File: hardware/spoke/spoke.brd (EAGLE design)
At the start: 45.7 x 44.1 mm, 23 parts, among them IC1 7805TV, IC2 LM3490, J1 AVR_SPI_PRG_6PTH, J2 POWER_JACKPTH, U1 ATMEGA328P_PDIP, U3 NRF24L01+

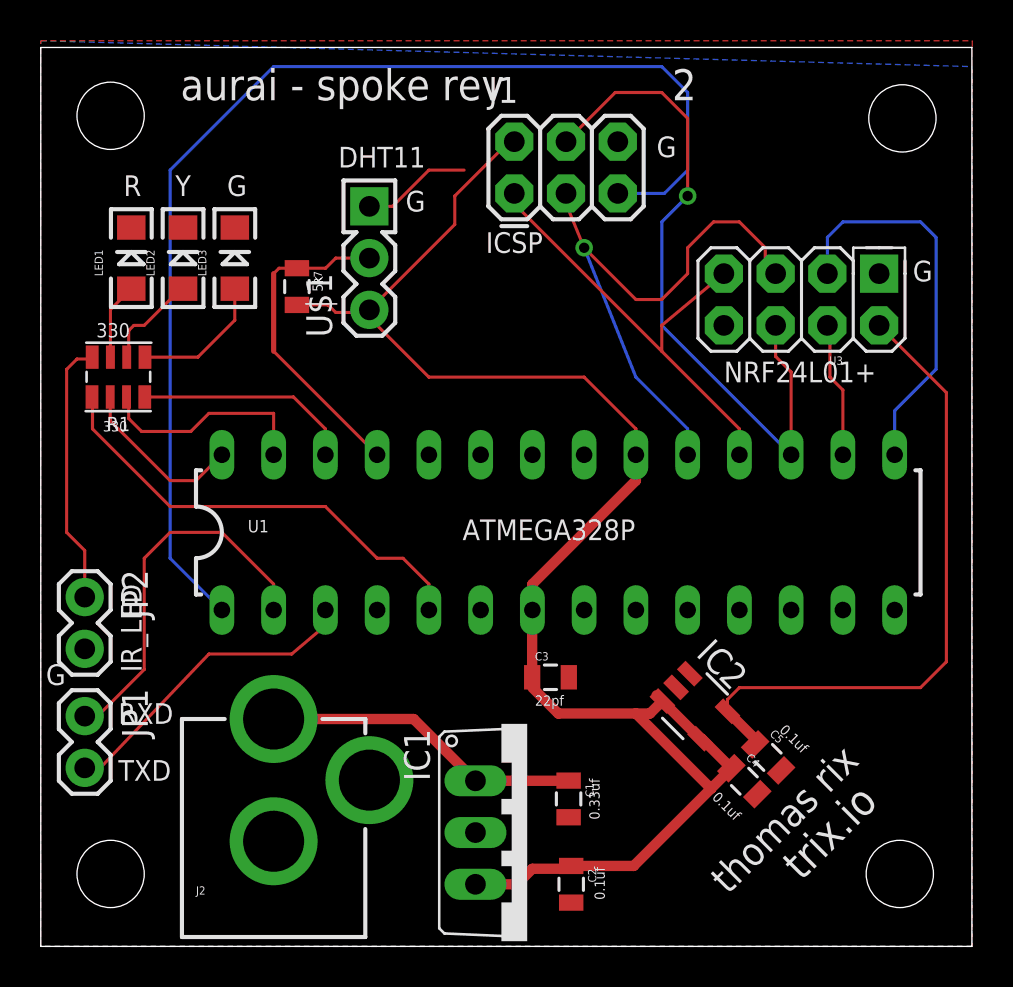
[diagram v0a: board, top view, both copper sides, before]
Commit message: Move from LM3490 to LM3940 regulator
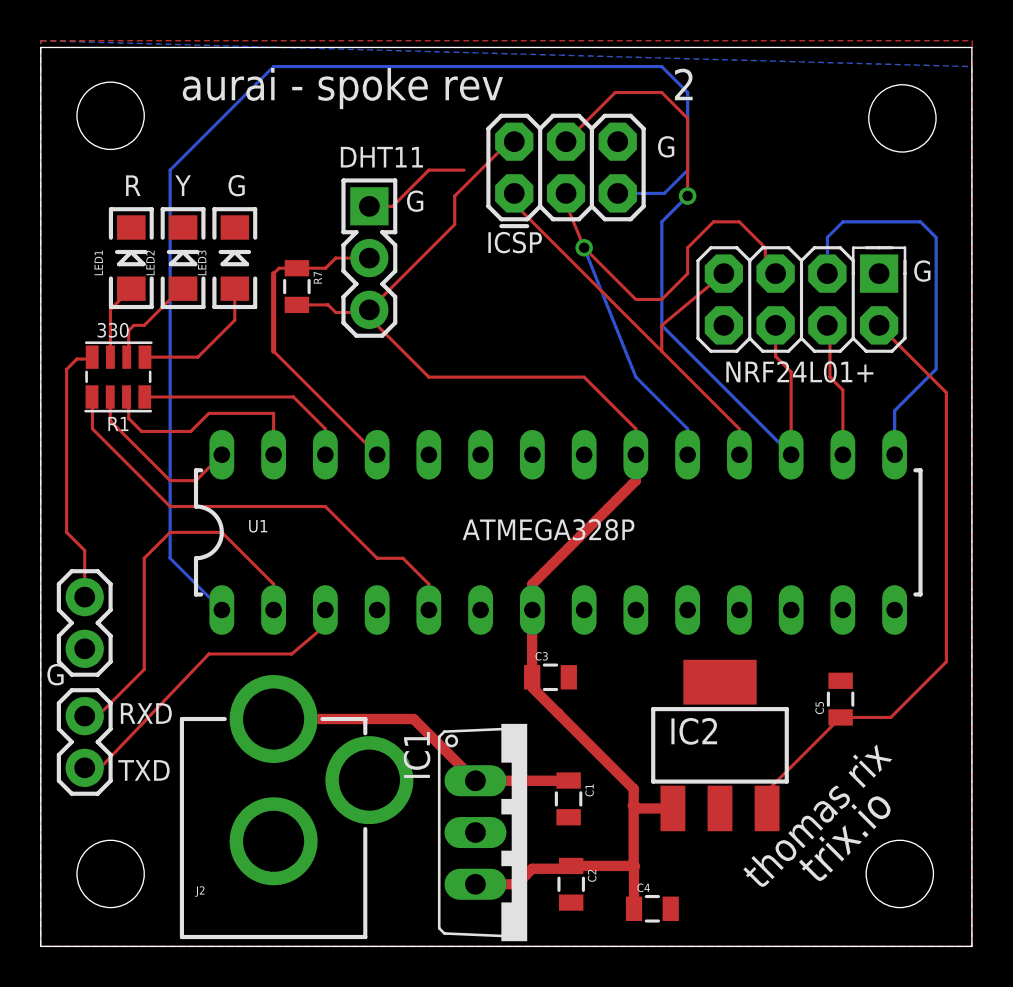
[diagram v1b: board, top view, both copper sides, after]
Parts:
- C4: value 0.1uF -> 0.47uF
- C5: value 0.1uF -> 33uF
- IC2: value LM3490 -> LM3940; device aurai:SOT23-5 -> aurai:SOT223
- moved C4 7.72 mm to (30.0, 1.85), turned to 0 degrees
- moved C5 4.56 mm to (39.3, 12.1), turned to 90 degrees
- moved IC2 2.28 mm to (33.3, 9.87), turned to 0 degrees
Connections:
- net 3.3V: now also IC2.3; no longer IC2.5
- net 5V: now also IC2.1; no longer IC2.3, IC2.4
- net GND: now also IC2.4
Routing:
- net 5V: track 78.1 -> 68.7 mm
- net 3.3V: track 32.2 -> 30.2 mm
- net N$2: track 17.9 -> 18.5 mm
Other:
- board text removed: "0.1uf"
- board text removed: "0.33uf"
- board text removed: "22pf"
- board text removed: "330"
- board text removed: "5k"
- board text removed: "IR_LED"
